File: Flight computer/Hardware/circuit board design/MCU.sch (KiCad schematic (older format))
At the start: 26 parts, among them J1 Conn_01x04, J2 Conn_01x02, U1 ATSAML21G18B-MUT, U7 W74M64FV, Y2 32.768KHz, Y3 16MHz

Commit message: created net list for first time
-changed SAML21 to J variant7
-filled in foot prints for all components exept comparator
-changed the footprints of ICSS pico tracker to a local copy
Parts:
- removed U1: ATSAML21G18B-MUT, Package_DFN_QFN:QFN-48-1EP_7x7mm_P0.5mm_EP5.15x5.15mm, symbol MCU_Microchip_SAML:ATSAML21G18B-MUT
- added U11: ATSAML21J18B-MUT, Package_DFN_QFN:QFN-64-1EP_9x9mm_P0.5mm_EP4.7x4.7mm, symbol MCU_Microchip_SAML:ATSAML21J18B-MUT
- BZ1: footprint (none) -> Buzzer_Beeper:Buzzer_12x9.5RM7.6
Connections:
- no-connect marks 2 -> 16
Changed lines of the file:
@@
-	1    0    0    -1
-$EndComp
-$Comp
-L MCU_Microchip_SAML:ATSAML21G18B-MUT U1
-U 1 1 5D6544DB
-P 6100 4400
-F 0 "U1" H 6650 6250 50  0000 C CNN
-F 1 "ATSAML21G18B-MUT" H 5400 2650 50  0000 C CNN
-F 2 "Package_DFN_QFN:QFN-48-1EP_7x7mm_P0.5mm_EP5.15x5.15mm" H 7400 6200 50  0001 C CNN
-F 3 "http://ww1.microchip.com/downloads/en/DeviceDoc/60001477A.pdf" H 6100 4400 50  0001 C CNN
-	1    6100 4400
 	1    0    0    -1
 $EndComp
@@
 F 0 "BZ1" H 8152 4729 50  0000 L CNN
 F 1 "Buzzer" H 8152 4638 50  0000 L CNN
-F 2 "" V 7975 4800 50  0001 C CNN
-F 3 "~" V 7975 4800 50  0001 C CNN
+F 2 "Buzzer_Beeper:Buzzer_12x9.5RM7.6" V 7975 4800 50  0001 C CNN
+F 3 "https://docs-emea.rs-online.com/webdocs/1581/0900766b815810c5.pdf" V 7975 4800 50  0001 C CNN
 	1    8000 4700
 	1    0    0    -1
@@
 Wire Wire Line
 	3900 4300 5100 4300
+$Comp
+L MCU_Microchip_SAML:ATSAML21J18B-MUT U11
+U 1 1 5D729B41
+P 6100 4400
+F 0 "U11" H 6100 2411 50  0000 C CNN
+F 1 "ATSAML21J18B-MUT" H 6100 2320 50  0000 C CNN
+F 2 "Package_DFN_QFN:QFN-64-1EP_9x9mm_P0.5mm_EP4.7x4.7mm" H 7400 6200 50  0001 C CNN
+F 3 "http://ww1.microchip.com/downloads/en/DeviceDoc/60001477A.pdf" H 6100 4400 50  0001 C CNN
+	1    6100 4400
+	1    0    0    -1
+$EndComp
+NoConn ~ 7100 5400
+NoConn ~ 7100 5300
+NoConn ~ 7100 5200
+NoConn ~ 7100 5100
+NoConn ~ 7100 5000
+NoConn ~ 7100 4900
+NoConn ~ 7100 4800
+NoConn ~ 7100 3900
+NoConn ~ 7100 3800
+NoConn ~ 7100 3700
+NoConn ~ 7100 3600
+NoConn ~ 7100 3500
+NoConn ~ 7100 3400
+NoConn ~ 7100 3300
 $EndSCHEMATC

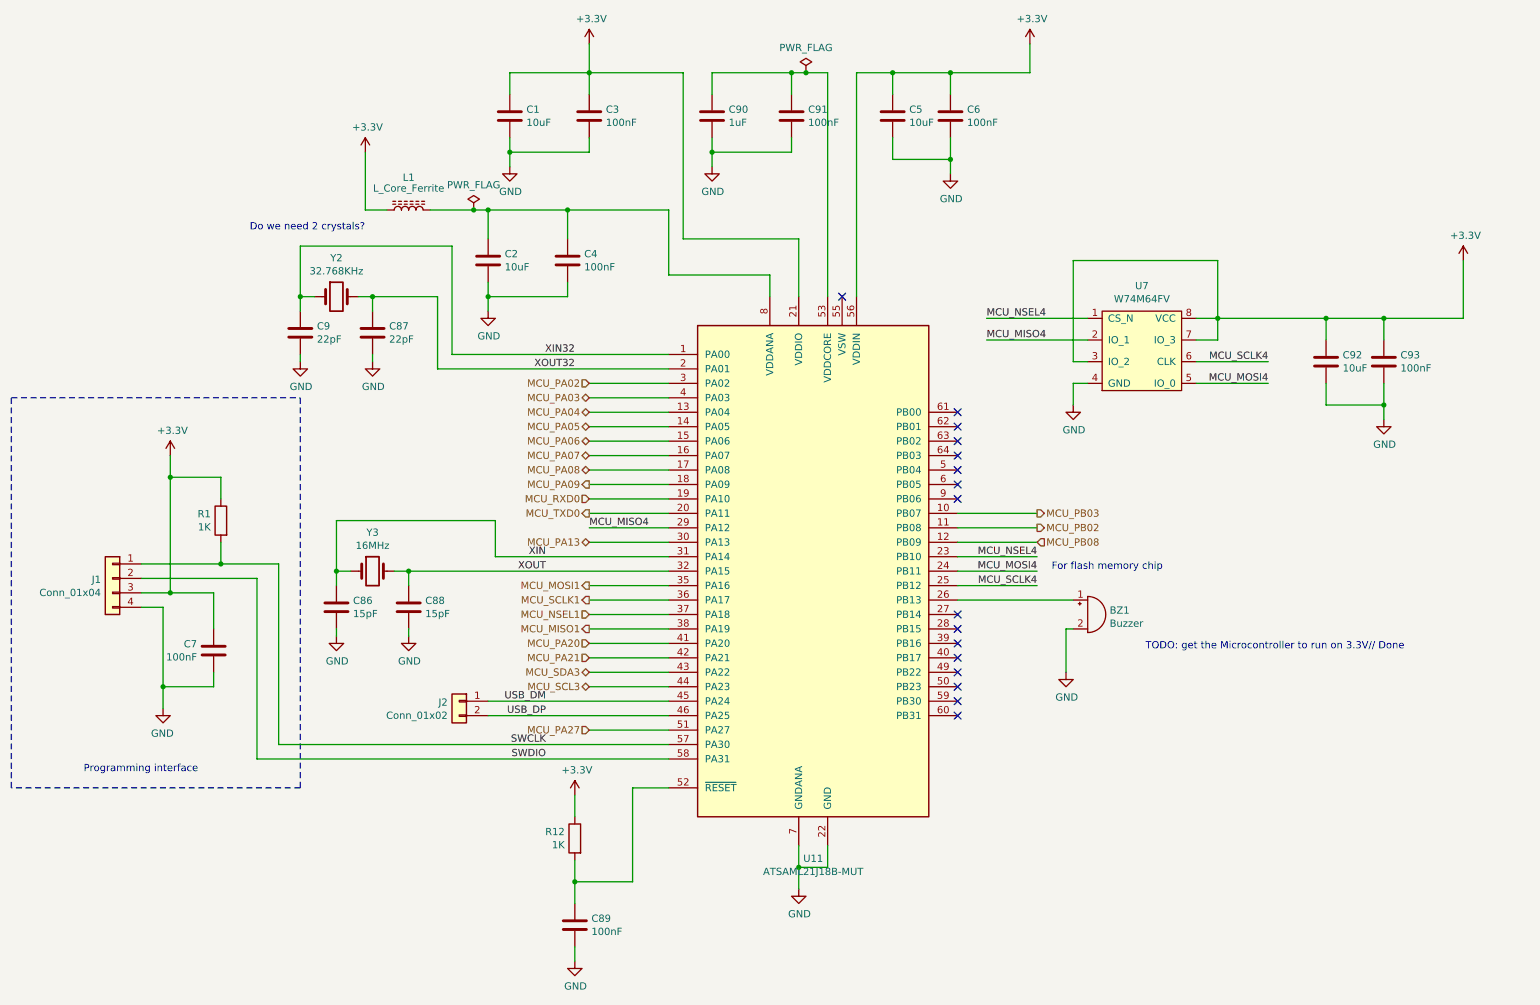
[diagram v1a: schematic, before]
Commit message: more upgrades
- removed the comparators
- added the cost and link to buy components
- added in a symbol for USB
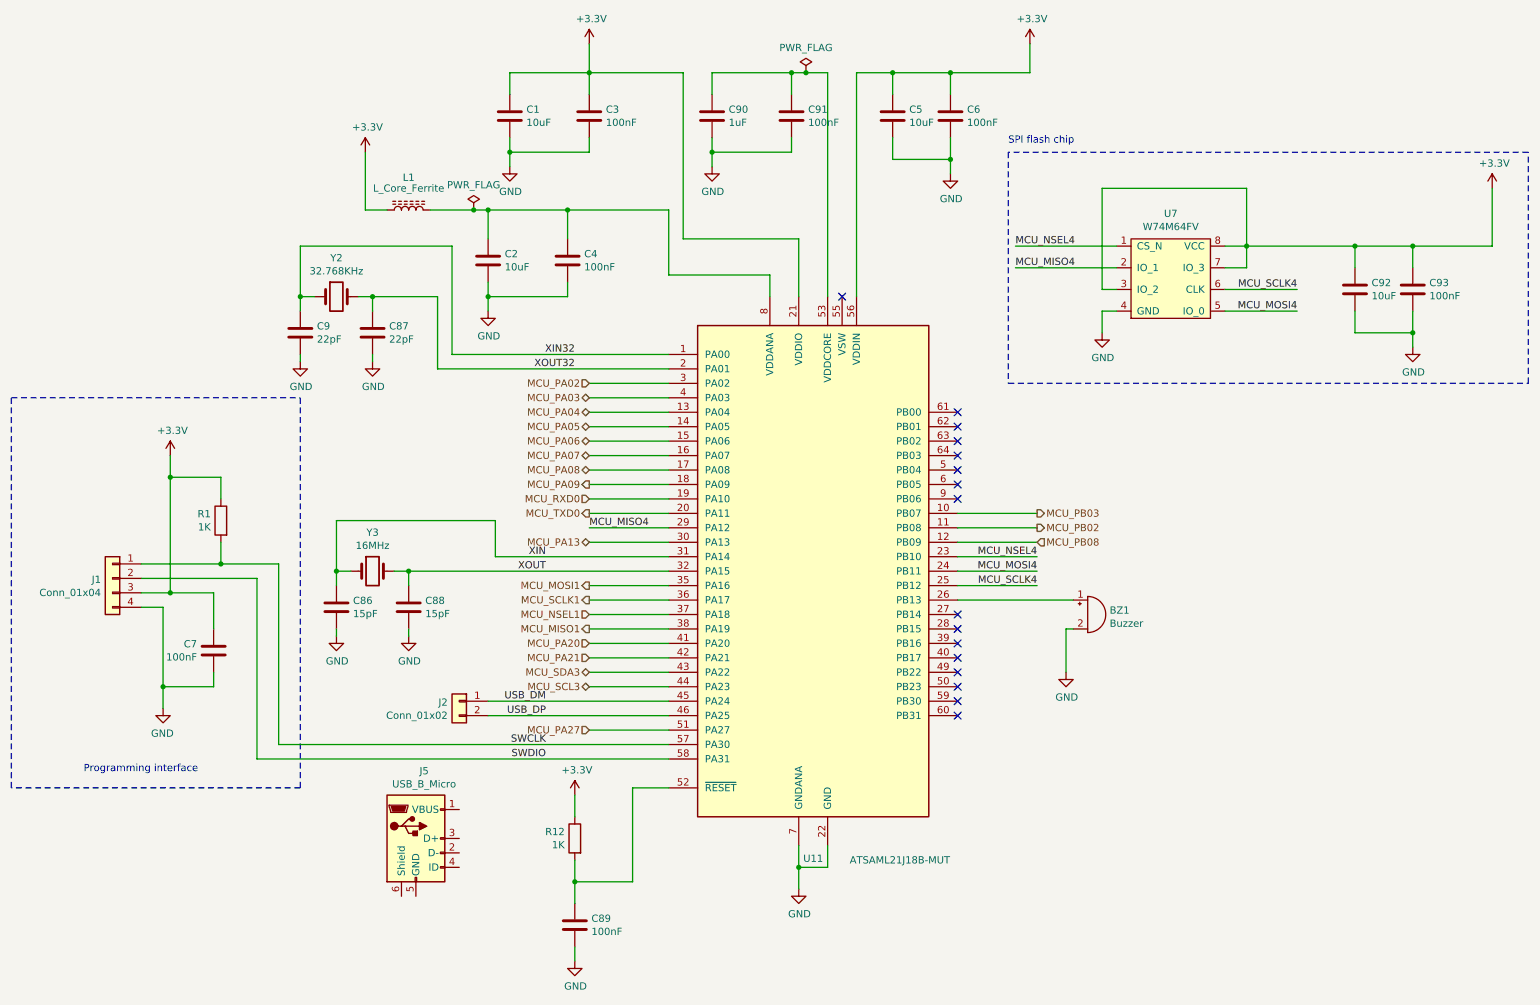
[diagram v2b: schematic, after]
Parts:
- added J5: USB_B_Micro, symbol Connector:USB_B_Micro
- BZ1: Cost (none) -> 1.05; Purchase link (none) -> https://uk.rs-online.com/web/p/magnetic-buzzer-components/6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
- U11: Cost (none) -> 4.07; Purchase link (none) -> https://www.mouser.co.uk/ProductDetail/Microchip-Technology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
- U7: Purchase link (none) -> https://www.mouser.co.uk/ProductDetail/Winbond/W74M64FVSSIQ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
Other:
- note added: "SPI flash chip"
- note removed: "Do we need 2 crystals?"
- note removed: "For flash memory chip\n"
- note removed: "TODO: get the Microcontroller to run on 3.3V// Done\n"
- moved on the sheet: C92, C93, U7
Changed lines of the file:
@@
 L power:GND #PWR050
 U 1 1 5DEA12DE
-P 7900 3250
-F 0 "#PWR050" H 7900 3000 50  0001 C CNN
-F 1 "GND" H 7905 3077 50  0000 C CNN
-F 2 "" H 7900 3250 50  0001 C CNN
-F 3 "" H 7900 3250 50  0001 C CNN
-	1    7900 3250
-	1    0    0    -1
-$EndComp
-Connection ~ 10050 2650
-Wire Wire Line
-	10050 2650 10600 2650
-Wire Wire Line
-	10050 2650 10050 2800
-Wire Wire Line
-	9650 2650 10050 2650
-Wire Wire Line
-	9650 2650 9650 2800
-Wire Wire Line
-	10050 3250 10050 3350
-Connection ~ 10050 3250
-Wire Wire Line
-	9650 3250 10050 3250
-Wire Wire Line
-	9650 3100 9650 3250
-Wire Wire Line
-	10050 3100 10050 3250
+P 8100 2750
+F 0 "#PWR050" H 8100 2500 50  0001 C CNN
+F 1 "GND" H 8105 2577 50  0000 C CNN
+F 2 "" H 8100 2750 50  0001 C CNN
+F 3 "" H 8100 2750 50  0001 C CNN
+	1    8100 2750
+	1    0    0    -1
+$EndComp
+Connection ~ 10250 2150
+Wire Wire Line
+	10250 2150 10800 2150
+Wire Wire Line
+	10250 2150 10250 2300
+Wire Wire Line
+	9850 2150 10250 2150
+Wire Wire Line
+	9850 2150 9850 2300
+Wire Wire Line
+	10250 2750 10250 2850
+Connection ~ 10250 2750
+Wire Wire Line
+	9850 2750 10250 2750
+Wire Wire Line
+	9850 2600 9850 2750
+Wire Wire Line
+	10250 2600 10250 2750
 $Comp
 L power:GND #PWR091
 U 1 1 5D640690
-P 10050 3350
-F 0 "#PWR091" H 10050 3100 50  0001 C CNN
-F 1 "GND" H 10055 3177 50  0000 C CNN
-F 2 "" H 10050 3350 50  0001 C CNN
-F 3 "" H 10050 3350 50  0001 C CNN
-	1    10050 3350
+P 10250 2850
+F 0 "#PWR091" H 10250 2600 50  0001 C CNN
+F 1 "GND" H 10255 2677 50  0000 C CNN
+F 2 "" H 10250 2850 50  0001 C CNN
+F 3 "" H 10250 2850 50  0001 C CNN
+	1    10250 2850
 	1    0    0    -1
 $EndComp
@@
 L Device:C C93
 U 1 1 5D64069A
-P 10050 2950
-F 0 "C93" H 10165 2996 50  0000 L CNN
-F 1 "100nF" H 10165 2905 50  0000 L CNN
-F 2 "Capacitor_SMD:C_0603_1608Metric" H 10088 2800 50  0001 C CNN
-F 3 "~" H 10050 2950 50  0001 C CNN
-	1    10050 2950
+P 10250 2450
+F 0 "C93" H 10365 2496 50  0000 L CNN
+F 1 "100nF" H 10365 2405 50  0000 L CNN
+F 2 "Capacitor_SMD:C_0603_1608Metric" H 10288 2300 50  0001 C CNN
+F 3 "~" H 10250 2450 50  0001 C CNN
+	1    10250 2450
 	1    0    0    -1
 $EndComp
@@
 L Device:C C92
 U 1 1 5D6406A4
-P 9650 2950
-F 0 "C92" H 9765 2996 50  0000 L CNN
-F 1 "10uF" H 9765 2905 50  0000 L CNN
-F 2 "Capacitor_SMD:C_0603_1608Metric" H 9688 2800 50  0001 C CNN
-F 3 "~" H 9650 2950 50  0001 C CNN
-	1    9650 2950
+P 9850 2450
+F 0 "C92" H 9965 2496 50  0000 L CNN
+F 1 "10uF" H 9965 2405 50  0000 L CNN
+F 2 "Capacitor_SMD:C_0603_1608Metric" H 9888 2300 50  0001 C CNN
+F 3 "~" H 9850 2450 50  0001 C CNN
+	1    9850 2450
 	1    0    0    -1
 $EndComp
@@
 MCU_PA02
 Wire Wire Line
-	8750 2650 8900 2650
-Connection ~ 9650 2650
-Wire Wire Line
-	8000 3100 7900 3100
-Wire Wire Line
-	7900 3100 7900 3250
+	8950 2150 9100 2150
+Connection ~ 9850 2150
+Wire Wire Line
+	8200 2600 8100 2600
+Wire Wire Line
+	8100 2600 8100 2750
 Wire Wire Line
 	7100 4400 7650 4400
@@
 	7100 4200 7650 4200
 Wire Wire Line
-	7900 2250 8900 2250
-Wire Wire Line
-	8900 2250 8900 2650
-Connection ~ 8900 2650
-Wire Wire Line
-	8000 2950 7900 2950
-Wire Wire Line
-	7900 2950 7900 2250
-Wire Wire Line
-	8750 2800 8900 2800
-Wire Wire Line
-	8900 2800 8900 2650
+	8100 1750 9100 1750
+Wire Wire Line
+	9100 1750 9100 2150
+Connection ~ 9100 2150
+Wire Wire Line
+	8200 2450 8100 2450
+Wire Wire Line
+	8100 2450 8100 1750
+Wire Wire Line
+	8950 2300 9100 2300
+Wire Wire Line
+	9100 2300 9100 2150
 Text Label 7650 4400 2    50   ~ 0
 MCU_MOSI4
 Text Label 7650 4500 2    50   ~ 0
 MCU_SCLK4
-Text Label 9250 2950 2    50   ~ 0
+Text Label 9450 2450 2    50   ~ 0
 MCU_SCLK4
 Wire Wire Line
-	8900 2650 9650 2650
-Wire Wire Line
-	8750 2950 9250 2950
-Wire Wire Line
-	8000 2650 7300 2650
-Wire Wire Line
-	8000 2800 7300 2800
-Wire Wire Line
-	8750 3100 9250 3100
-Text Label 7300 2800 0    50   ~ 0
+	9100 2150 9850 2150
+Wire Wire Line
+	8950 2450 9450 2450
+Wire Wire Line
+	8200 2150 7500 2150
+Wire Wire Line
+	8200 2300 7500 2300
+Wire Wire Line
+	8950 2600 9450 2600
+Text Label 7500 2300 0    50   ~ 0
 MCU_MISO4
-Text Label 7300 2650 0    50   ~ 0
+Text Label 7500 2150 0    50   ~ 0
 MCU_NSEL4
-Text Label 9250 3100 2    50   ~ 0
+Text Label 9450 2600 2    50   ~ 0
 MCU_MOSI4
 Text HLabel 4550 4200 0    50   BiDi ~ 0
@@
 Text Label 4550 4100 0    50   ~ 0
 MCU_MISO4
-Text Notes 8400 4950 0    50   ~ 0
-TODO: get the Microcontroller to run on 3.3V// Done\n
 $Comp
 L Device:Buzzer BZ1
@@
 F 2 "Buzzer_Beeper:Buzzer_12x9.5RM7.6" V 7975 4800 50  0001 C CNN
 F 3 "https://docs-emea.rs-online.com/webdocs/1581/0900766b815810c5.pdf" V 7975 4800 50  0001 C CNN
+F 4 "1.05" H 8000 4700 50  0001 C CNN "Cost"
+F 5 "https://uk.rs-online.com/web/p/magnetic-buzzer-components/6173081/?searchTerm=6173081&relevancy-data=636F3D3126696E3D4931384E525353746F636B4E756D6265724D504E266C753D656E266D6D3D6D61746368616C6C26706D3D5E5C647B367D247C5E5C647B377D247C5E5C647B31307D2426706F3D313426736E3D592673743D52535F53544F434B5F4E554D4245522677633D4E4F4E45267573743D3631373330383126" H 8000 4700 50  0001 C CNN "Purchase link"
 	1    8000 4700
 	1    0    0    -1
@@
 L power:+3.3V #PWR022
 U 1 1 5D667177
-P 10600 2250
-F 0 "#PWR022" H 10600 2100 50  0001 C CNN
-F 1 "+3.3V" H 10615 2423 50  0000 C CNN
-F 2 "" H 10600 2250 50  0001 C CNN
-F 3 "" H 10600 2250 50  0001 C CNN
-	1    10600 2250
-	1    0    0    -1
-$EndComp
-Wire Wire Line
-	10600 2650 10600 2250
+P 10800 1750
+F 0 "#PWR022" H 10800 1600 50  0001 C CNN
+F 1 "+3.3V" H 10815 1923 50  0000 C CNN
+F 2 "" H 10800 1750 50  0001 C CNN
+F 3 "" H 10800 1750 50  0001 C CNN
+	1    10800 1750
+	1    0    0    -1
+$EndComp
+Wire Wire Line
+	10800 2150 10800 1750
 $Comp
 L power:+3.3V #PWR020
@@
 Text Notes 1050 5800 0    50   ~ 0
 Programming interface\n
-Text Notes 7750 4400 0    50   ~ 0
-For flash memory chip\n
 $Comp
 L power:+3.3V #PWR0102
@@
 	0    -1   -1   0
 $EndComp
-Text Notes 2200 2050 0    50   ~ 0
-Do we need 2 crystals?
 Text HLabel 4550 4900 0    50   Input ~ 0
 MCU_PA20
@@
 L flight-computer:W74M64FV U7
 U 1 1 5D77FBCE
-P 8100 3150
-F 0 "U7" H 8375 3875 50  0000 C CNN
-F 1 "W74M64FV" H 8375 3784 50  0000 C CNN
-F 2 "Package_SO:SOIC-8_5.23x5.23mm_P1.27mm" H 8100 3150 50  0001 C CNN
-F 3 "https://docs-emea.rs-online.com/webdocs/1623/0900766b81623058.pdf" H 8100 3150 50  0001 C CNN
-	1    8100 3150
+P 8300 2650
+F 0 "U7" H 8575 3375 50  0000 C CNN
+F 1 "W74M64FV" H 8575 3284 50  0000 C CNN
+F 2 "Package_SO:SOIC-8_5.23x5.23mm_P1.27mm" H 8300 2650 50  0001 C CNN
+F 3 "https://docs-emea.rs-online.com/webdocs/1623/0900766b81623058.pdf" H 8300 2650 50  0001 C CNN
+F 4 "https://www.mouser.co.uk/ProductDetail/Winbond/W74M64FVSSIQ?qs=qSfuJ%252Bfl%2Fd52YBej%252Bs3iEg==" H 8300 2650 50  0001 C CNN "Purchase link"
+	1    8300 2650
 	1    0    0    -1
 $EndComp
@@
 P 6100 4400
 F 0 "U11" H 6100 2411 50  0000 C CNN
-F 1 "ATSAML21J18B-MUT" H 6100 2320 50  0000 C CNN
+F 1 "ATSAML21J18B-MUT" H 6700 2400 50  0000 C CNN
 F 2 "Package_DFN_QFN:QFN-64-1EP_9x9mm_P0.5mm_EP4.7x4.7mm" H 7400 6200 50  0001 C CNN
 F 3 "http://ww1.microchip.com/downloads/en/DeviceDoc/60001477A.pdf" H 6100 4400 50  0001 C CNN
+F 4 "4.07" H 6100 4400 50  0001 C CNN "Cost"
+F 5 "https://www.mouser.co.uk/ProductDetail/Microchip-Technology/ATSAML21J18B-MUT?qs=RCSZh%2F2c5nc%252BoA8shEl23w==" H 6100 4400 50  0001 C CNN "Purchase link"
 	1    6100 4400
 	1    0    0    -1
@@
 NoConn ~ 7100 3400
 NoConn ~ 7100 3300
+$Comp
+L Connector:USB_B_Micro J5
+U 1 1 5D7395BE
+P 3350 6250
+F 0 "J5" H 3407 6717 50  0000 C CNN
+F 1 "USB_B_Micro" H 3407 6626 50  0000 C CNN
+F 2 "" H 3500 6200 50  0001 C CNN
+F 3 "~" H 3500 6200 50  0001 C CNN
+	1    3350 6250
+	1    0    0    -1
+$EndComp
+Wire Notes Line
+	7450 1500 7450 3100
+Wire Notes Line
+	7450 3100 11050 3100
+Wire Notes Line
+	11050 3100 11050 1500
+Wire Notes Line
+	11050 1500 7450 1500
+Text Notes 7450 1450 0    50   ~ 0
+SPI flash chip
 $EndSCHEMATC
